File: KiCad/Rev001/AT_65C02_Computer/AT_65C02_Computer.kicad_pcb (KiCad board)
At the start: 2 copper layers, 203.2 x 149.9 mm, 123 parts, among them J1 CLK Jumper, J11 LCD Connector, J12 Expansion port #2, J14 ESP Interface, J15 Level_Shifter_HV, J16 Level_Shifter_LV, J18 CPU Signals, J19 Address Decoder Enable, J2 Optional UART Port, J3 Conn_01x06_Female, J5 Barrel_Jack-Connector, J6 Mini-DIN-6, J7 Expansion port, J8 AVR-ISP-10, J9 VIA2PA - VIA2PB, SW1 SW_SPDT, SW2 Step, SW3 Mode, SW4 SW_SPDT, U1 74HC21, U10 ATtiny4313-PU, U11 65C22S, U12 65C22S, U13 L7806, U14 74LS04, U15 74LS08, U16 74LS32, U17 NE555, U18 NE555, U19 NE555, U2 74HC00, U20 74HCT540, U21 74HCT573, U22 74HCT573, U23 74HCT573, U24 10_LED_Array, U25 10_LED_Array, U26 10_LED_Array, U27 10_LED_Array, U3 74HC02, U4 NE555, U5 65C51N, U6 Regulator_Linear_L7805, U7 65C02S, U8 28C256, U9 62256, X1 1MHz, X2 1.8432MHz

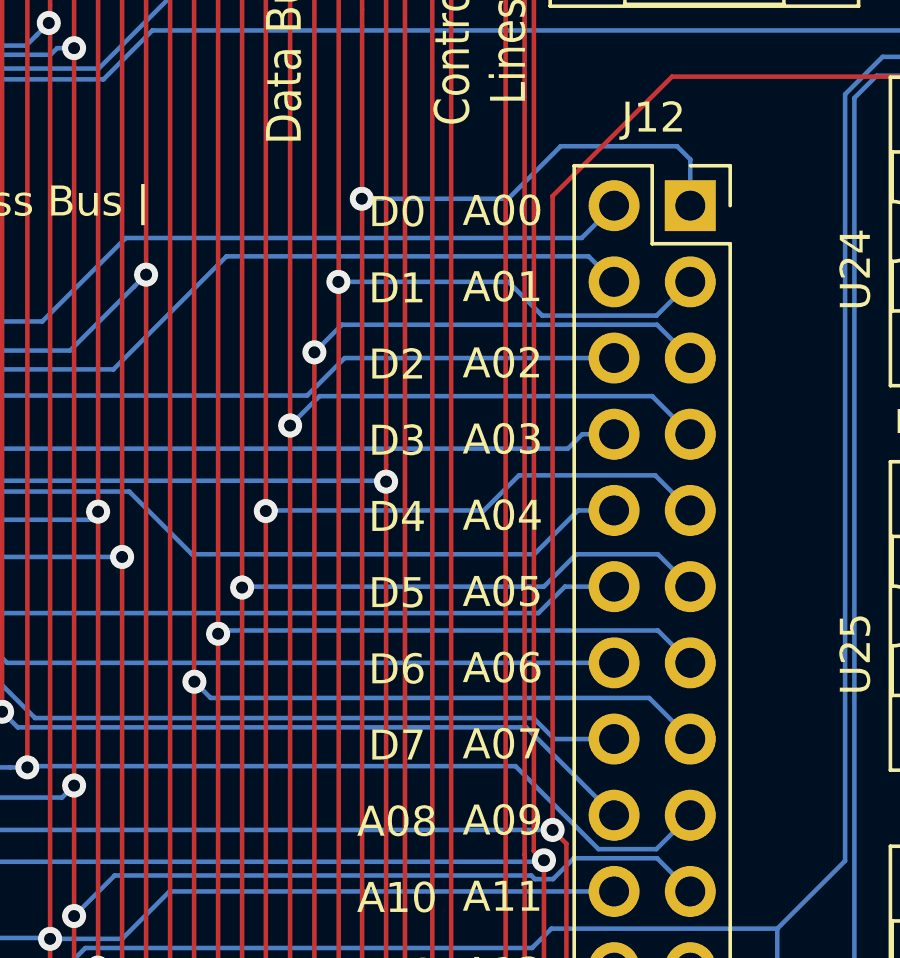
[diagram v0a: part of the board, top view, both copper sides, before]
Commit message: Silk Screen Modifications - Hex Display WIP
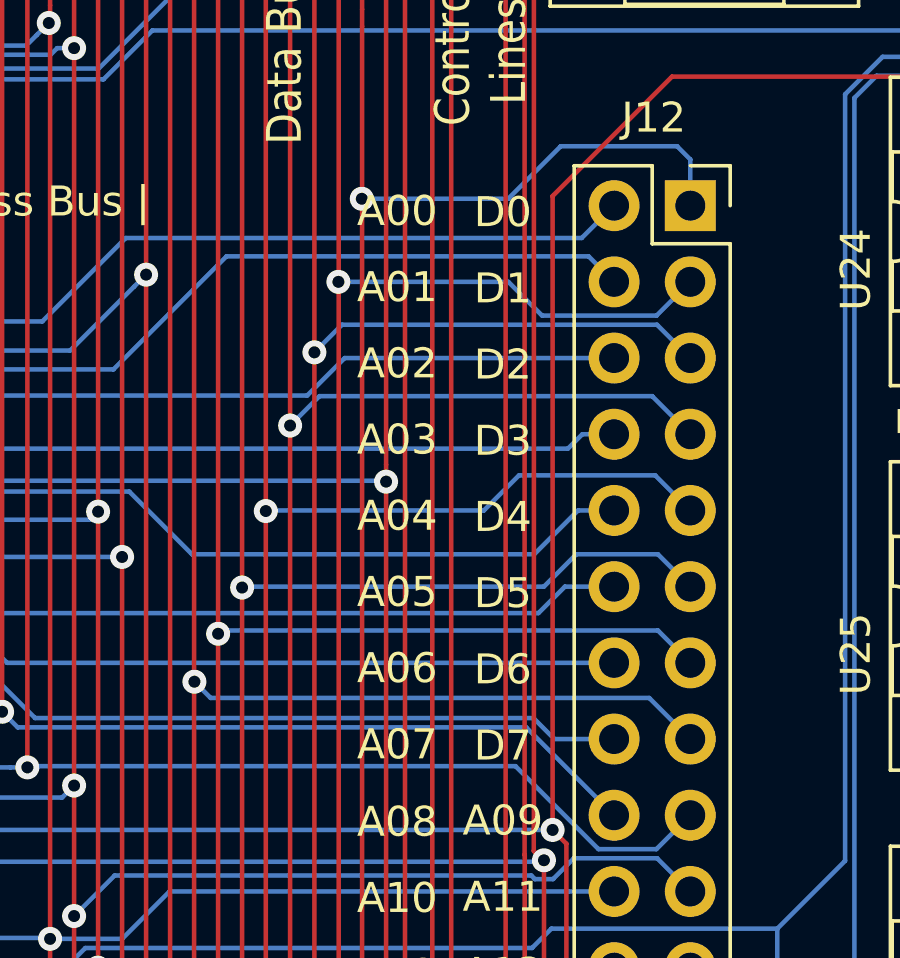
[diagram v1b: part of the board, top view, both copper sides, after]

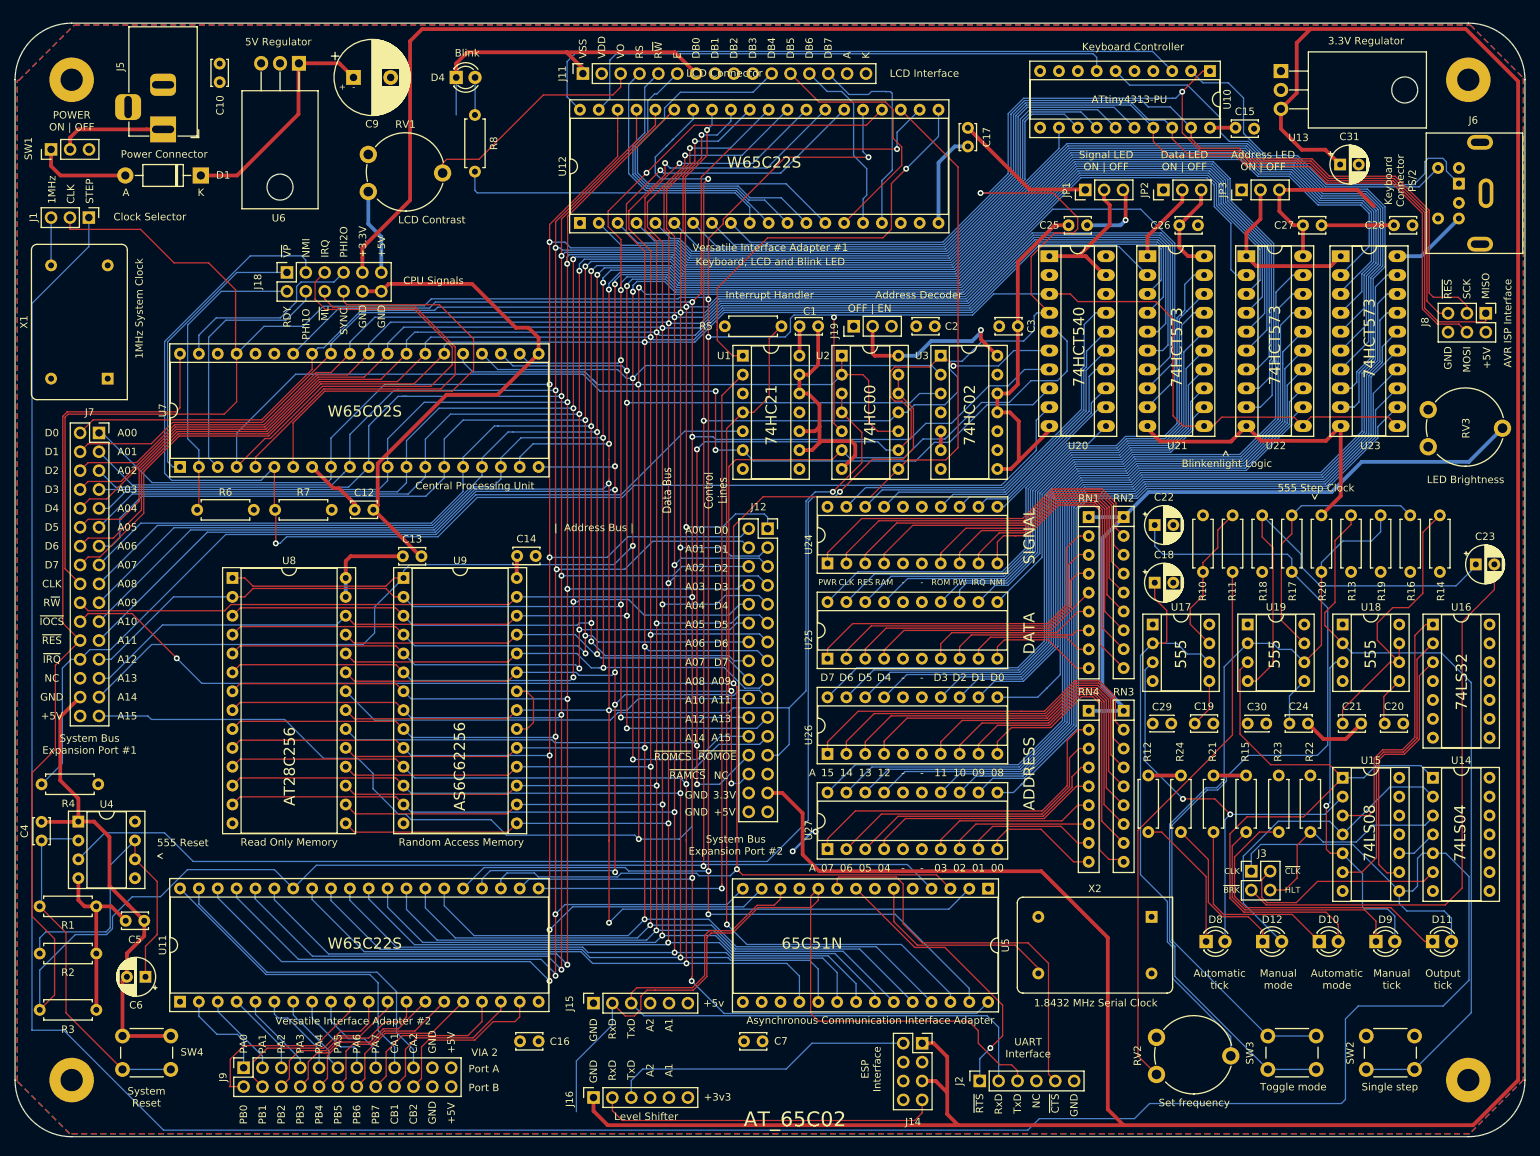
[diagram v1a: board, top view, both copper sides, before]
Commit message: HEX Board Mods
Hex board changes. Main board Hex to Latches
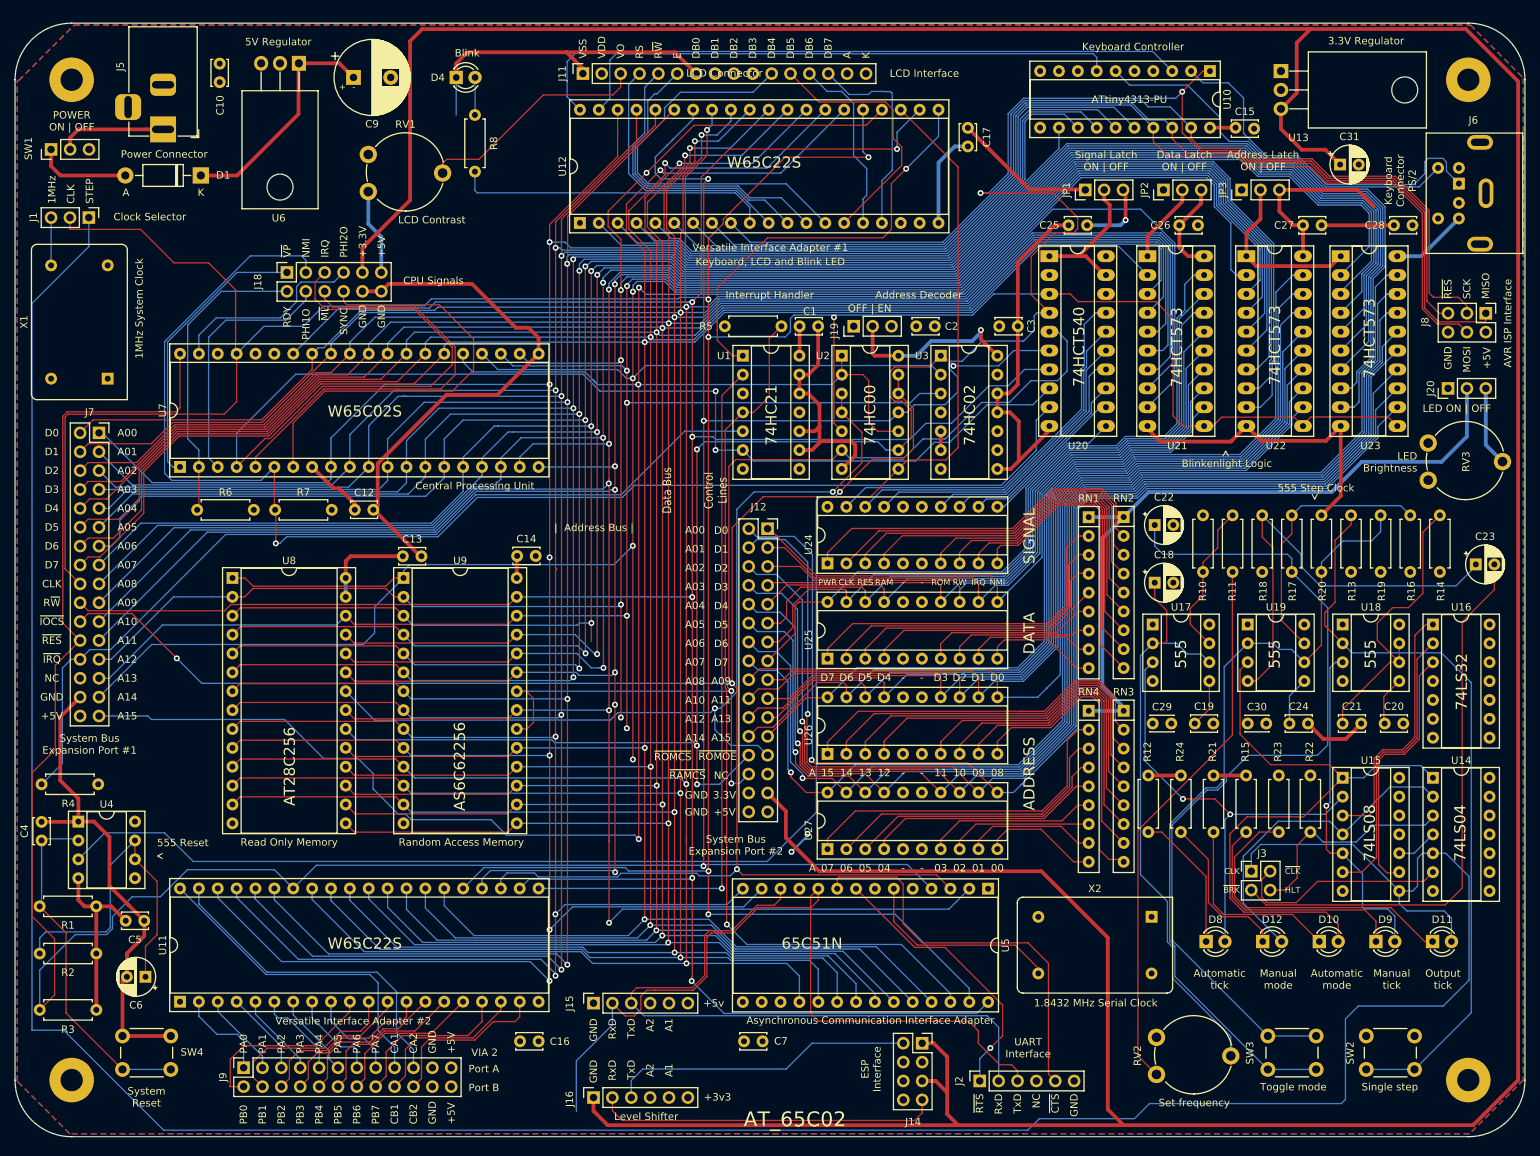
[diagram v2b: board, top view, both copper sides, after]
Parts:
- added J20: LED SWITCH, Connector_PinHeader_2.54mm:PinHeader_1x03_P2.54mm_Vertical, F.Cu at (210.6, 69.5)
- moved RV3 4.50 mm to (208.0, 81.8)
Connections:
- J12 pad 1: d0 -> db0
- J12 pad 10: a4 -> ab4
- J12 pad 11: d5 -> db5
- J12 pad 12: a5 -> ab5
- J12 pad 13: d6 -> db6
- J12 pad 14: a6 -> ab6
- J12 pad 15: d7 -> db7
- J12 pad 16: a7 -> ab7
- J12 pad 17: a9 -> ab9
- J12 pad 18: a8 -> ab8
- J12 pad 19: a11 -> ab11
- J12 pad 2: a0 -> ab0
- J12 pad 20: a10 -> ab10
- J12 pad 21: a13 -> ab13
- J12 pad 22: a12 -> ab12
- J12 pad 23: a15 -> ab15
- J12 pad 24: a14 -> ab14
- J12 pad 3: d1 -> db1
- J12 pad 4: a1 -> ab1
- J12 pad 5: d2 -> db2
- J12 pad 6: a2 -> ab2
- J12 pad 7: d3 -> db3
- J12 pad 8: a3 -> ab3
- J12 pad 9: d4 -> db4
- RV3 pad 2: LED_bright -> Net-(J20-Pad3)
- U21 pad 12: Net-(U21-Pad12) -> db0
- U21 pad 13: Net-(U21-Pad13) -> db1
- U21 pad 14: Net-(U21-Pad14) -> db2
- U21 pad 15: Net-(U21-Pad15) -> db3
- U21 pad 16: Net-(U21-Pad16) -> db4
- U21 pad 17: Net-(U21-Pad17) -> db5
- U21 pad 18: Net-(U21-Pad18) -> db6
- U21 pad 19: Net-(U21-Pad19) -> db7
- U22 pad 12: Net-(U22-Pad12) -> ab8
- U22 pad 13: Net-(U22-Pad13) -> ab9
- U22 pad 14: Net-(U22-Pad14) -> ab10
- U22 pad 15: Net-(U22-Pad15) -> ab11
- U22 pad 16: Net-(U22-Pad16) -> ab12
- U22 pad 17: Net-(U22-Pad17) -> ab13
- U22 pad 18: Net-(U22-Pad18) -> ab14
- U22 pad 19: Net-(U22-Pad19) -> ab15
- U23 pad 12: Net-(U23-Pad12) -> ab0
- U23 pad 13: Net-(U23-Pad13) -> ab1
- U23 pad 14: Net-(U23-Pad14) -> ab2
- U23 pad 15: Net-(U23-Pad15) -> ab3
- U23 pad 16: Net-(U23-Pad16) -> ab4
- U23 pad 17: Net-(U23-Pad17) -> ab5
- U23 pad 18: Net-(U23-Pad18) -> ab6
- U23 pad 19: Net-(U23-Pad19) -> ab7
- U25 pad 11: Net-(U21-Pad12) -> db0
- U25 pad 12: Net-(U21-Pad13) -> db1
- U25 pad 13: Net-(U21-Pad14) -> db2
- U25 pad 14: Net-(U21-Pad15) -> db3
- U25 pad 17: Net-(U21-Pad16) -> db4
- U25 pad 18: Net-(U21-Pad17) -> db5
- U25 pad 19: Net-(U21-Pad18) -> db6
- U25 pad 20: Net-(U21-Pad19) -> db7
- U26 pad 11: Net-(U22-Pad12) -> ab8
- U26 pad 12: Net-(U22-Pad13) -> ab9
- U26 pad 13: Net-(U22-Pad14) -> ab10
- U26 pad 14: Net-(U22-Pad15) -> ab11
- U26 pad 17: Net-(U22-Pad16) -> ab12
- U26 pad 18: Net-(U22-Pad17) -> ab13
- U26 pad 19: Net-(U22-Pad18) -> ab14
- U26 pad 20: Net-(U22-Pad19) -> ab15
- U27 pad 11: Net-(U23-Pad12) -> ab0
- U27 pad 12: Net-(U23-Pad13) -> ab1
- U27 pad 13: Net-(U23-Pad14) -> ab2
- U27 pad 14: Net-(U23-Pad15) -> ab3
- U27 pad 17: Net-(U23-Pad16) -> ab4
- U27 pad 18: Net-(U23-Pad17) -> ab5
- U27 pad 19: Net-(U23-Pad18) -> ab6
- U27 pad 20: Net-(U23-Pad19) -> ab7
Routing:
- net ab1: track 0.00 -> 159.6 mm, vias 0 -> 1
- net ab7: track 0.00 -> 158.3 mm, vias 0 -> 1
- net ab0: track 0.00 -> 158.2 mm, vias 0 -> 1
- net ab6: track 0.00 -> 158.1 mm, vias 0 -> 1
- net ab5: track 0.00 -> 158.0 mm, vias 0 -> 1
- net ab3: track 0.00 -> 157.1 mm, vias 0 -> 1
- net ab4: track 0.00 -> 156.9 mm, vias 0 -> 1
- net ab2: track 0.00 -> 156.7 mm, vias 0 -> 1
- net Net-(U23-Pad19): track 133.0 -> 0.00 mm
- net Net-(U23-Pad18): track 128.2 -> 0.00 mm
- net Net-(U23-Pad17): track 123.4 -> 0.00 mm
- net ab14: track 0.00 -> 122.1 mm
- net ab15: track 0.00 -> 119.2 mm
- net Net-(U23-Pad16): track 117.8 -> 0.00 mm
- net ab12: track 0.00 -> 116.4 mm
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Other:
- board text added: "Address Latch ON | OFF"
- board text added: "Data Latch ON | OFF"
- board text added: "LED ON | OFF"
- board text added: "Signal Latch ON | OFF"
- board text removed: "Address LED ON | OFF"
- board text removed: "Data LED ON | OFF"
- board text removed: "Signal LED ON | OFF"
